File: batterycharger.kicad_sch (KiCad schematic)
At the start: 0 parts

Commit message: added
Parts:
- added U1: LT3652EMSE, Package_SO:MSOP-12-1EP_3x4mm_P0.65mm_EP1.65x2.85mm, symbol Battery_Management:LT3652EMSE
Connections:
- new net gnd: U1.13 (GND)
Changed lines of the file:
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@@
 (kicad_sch (version 20230121) (generator eeschema)
   (paper "A4")
-  (hierarchical_label "in" (shape input) (at 78.74 87.63 0) (fields_autoplaced)
+  (wire (pts (xy 63.5 107.95) (xy 87.63 107.95))
+    (stroke (width 0) (type default))
+  )
+  (wire (pts (xy 63.5 93.98) (xy 63.5 107.95))
+    (stroke (width 0) (type default))
+  )
+  (hierarchical_label "in" (shape input) (at 63.5 87.63 0) (fields_autoplaced)
     (effects (font (size 1.27 1.27)) (justify left))
   )
-  (hierarchical_label "load" (shape output) (at 95.25 87.63 0) (fields_autoplaced)
+  (hierarchical_label "gnd" (shape input) (at 63.5 93.98 0) (fields_autoplaced)
     (effects (font (size 1.27 1.27)) (justify left))
   )
+  (hierarchical_label "load" (shape output) (at 106.68 87.63 0) (fields_autoplaced)
+    (effects (font (size 1.27 1.27)) (justify left))
+  )
+  (symbol (lib_id "Battery_Management:LT3652EMSE") (at 87.63 95.25 0) (unit 1)
+    (in_bom yes) (on_board yes) (dnp no) (fields_autoplaced)
+    (property "Reference" "U1" (at 89.8241 80.01 0)
+      (effects (font (size 1.27 1.27)) (justify left))
+    )
+    (property "Value" "LT3652EMSE" (at 89.8241 82.55 0)
+      (effects (font (size 1.27 1.27)) (justify left))
+    )
+    (property "Footprint" "Package_SO:MSOP-12-1EP_3x4mm_P0.65mm_EP1.65x2.85mm" (at 87.63 110.49 0)
+      (effects (font (size 1.27 1.27)) hide)
+    )
+    (property "Datasheet" "https://www.analog.com/media/en/technical-documentation/data-sheets/3652fe.pdf" (at 102.87 115.57 0)
+      (effects (font (size 1.27 1.27)) hide)
+    )
+    (pin "1")
+    (pin "10")
+    (pin "11")
+    (pin "12")
+    (pin "13")
+    (pin "2")
+    (pin "3")
+    (pin "4")
+    (pin "5")
+    (pin "6")
+    (pin "7")
+    (pin "8")
+    (pin "9")
+    (instances
+      (project "eps"
+        (path "/d1becec8-2a81-45a7-bfc6-f9ad93456edc/a41c2f06-c716-4d4c-abbd-50372b3cec58"
+          (reference "U1") (unit 1)
+        )
+        (path "/d1becec8-2a81-45a7-bfc6-f9ad93456edc/98043307-5f00-404c-bb35-46ff24bbd3b8"
+          (reference "U2") (unit 1)
+        )
+      )
+    )
+  )
 )

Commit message: v0.1Hydrogen
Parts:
- added BT1, BT2, BT3, BT4: Battery_Cell, Battery:BatteryHolder_Keystone_1042_1x18650, symbol Device:Battery_Cell
- added C1, C4: 10uF, Capacitor_THT:C_Disc_D5.1mm_W3.2mm_P5.00mm, symbol Device:C
- added C2: 100uF, Capacitor_THT:CP_Radial_D6.3mm_P2.50mm, symbol Device:C_Polarized
- added C3: 1uF, Capacitor_THT:C_Disc_D5.0mm_W2.5mm_P2.50mm, symbol Device:C
- added C5: 100uF 16v, Capacitor_THT:CP_Radial_D6.3mm_P2.50mm, symbol Device:C_Polarized
- added D10, D9: LED, LED_THT:LED_Rectangular_W3.0mm_H2.0mm, symbol Device:LED
- added D11, D12, D13, D7, D8: 1N5819, Diode_THT:D_DO-41_SOD81_P10.16mm_Horizontal, symbol Diode:1N5819
- added J1: Barrel_Jack, Connector_BarrelJack:BarrelJack_SwitchcraftConxall_RAPC10U_Horizontal, symbol Connector:Barrel_Jack
- added L1: 68uH, Inductor_THT:L_Axial_L5.0mm_D3.6mm_P10.00mm_Horizontal_Murata_BL01RN1A2A2, symbol Device:L
- added R1: 568k, Resistor_THT:R_Axial_DIN0204_L3.6mm_D1.6mm_P5.08mm_Horizontal, symbol Device:R
- added R2, R3: 1k, Resistor_THT:R_Axial_DIN0204_L3.6mm_D1.6mm_P5.08mm_Horizontal, symbol Device:R
- added R4: 0.22, Resistor_THT:R_Axial_DIN0204_L3.6mm_D1.6mm_P5.08mm_Horizontal, symbol Device:R
- added R5: 0.5, Resistor_THT:R_Axial_DIN0204_L3.6mm_D1.6mm_P5.08mm_Horizontal, symbol Device:R
- added R6: 446k, Resistor_THT:R_Axial_DIN0204_L3.6mm_D1.6mm_P5.08mm_Horizontal, symbol Device:R
- added R7: 200k, Resistor_THT:R_Axial_DIN0204_L3.6mm_D1.6mm_P5.08mm_Horizontal, symbol Device:R
- added RV1: 10k, Potentiometer_THT:Potentiometer_Bourns_3386P_Vertical, symbol Device:R_Potentiometer
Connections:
- net gnd is gone; now on net GND: U1.13 (GND)
- net in: now also U1.1 (V_{IN}), U1.3 (~{SHDN}), C1.1, D10.2 (A), D12.2 (A), D7.1 (K), D9.2 (A), RV1.1
- net load: now also D12.1 (K), D13.1 (K)
- net at U1.10 (SENSE): now also L1.2, R4.1, R5.2
- net at U1.11 (BOOST): now also C3.1, D11.1 (K)
- net at U1.12 (SW): now also C3.2, D8.1 (K), L1.1
- net at U1.2 (V_{IN_REG}): now also RV1.2
- net chrg: now reaches U1.4 (~{CHRG})
- net chrg: now also R3.1
- net fault: now reaches U1.5 (~{FAULT})
- net fault: now also R2.1
- net GND: now reaches U1.6 (TIMER)
- net GND: now also BT3.2 (-), BT4.2 (-), C1.2, C2.2, C4.2, C5.2, D8.2 (A), J1.2, R6.2, RV1.3
- net at U1.7 (V_{FB}): now also R7.1
- net at U1.9 (BAT): now also BT1.1 (+), BT2.1 (+), C2.1, C4.1, C5.1, D11.2 (A), D13.2 (A), R1.1, R4.2, R5.1
- new net: D7.2 (A), J1.1
- new net: R1.2, R6.1, R7.2
- new net: D10.1 (K), R3.2
- new net: D9.1 (K), R2.2
- new net: BT2.2 (-), BT4.1 (+)
- new net: BT1.2 (-), BT3.1 (+)
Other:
- moved on the sheet: U1

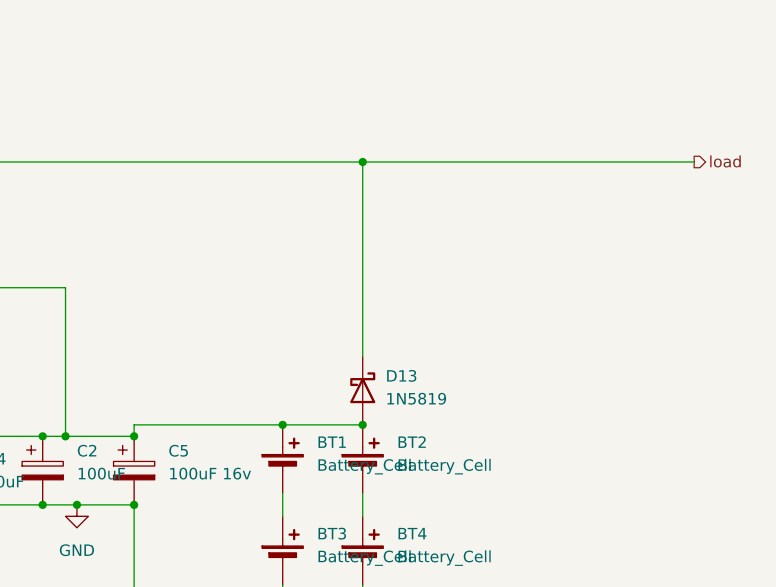
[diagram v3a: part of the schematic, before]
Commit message: Adding sensors
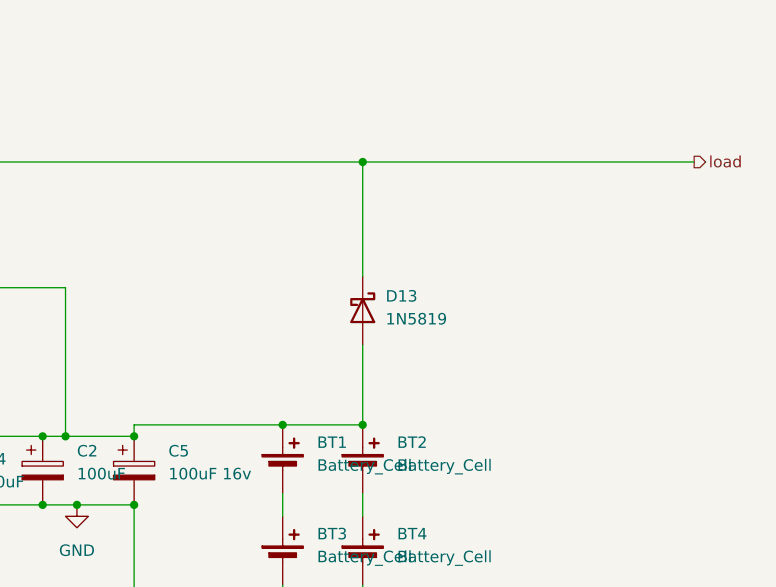
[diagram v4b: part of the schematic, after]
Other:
- moved on the sheet: D13
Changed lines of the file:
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@@
 	(wire
 		(pts
-			(xy 204.47 78.74) (xy 204.47 57.15)
+			(xy 204.47 69.85) (xy 204.47 57.15)
+		)
+		(stroke
+			(width 0)
+			(type default)
+		)
+	)
+	(wire
+		(pts
+			(xy 204.47 77.47) (xy 204.47 86.36)
 		)
 		(stroke
@@
 	(symbol
 		(lib_id "Diode:1N5819")
-		(at 204.47 82.55 270)
+		(at 204.47 73.66 270)
 		(unit 1)
 		(exclude_from_sim no)
@@
 		(fields_autoplaced yes)
 		(property "Reference" "D13"
-			(at 207.01 80.9625 90)
+			(at 207.01 72.0725 90)
 			(effects
 				(font
@@
 		)
 		(property "Value" "1N5819"
-			(at 207.01 83.5025 90)
+			(at 207.01 74.6125 90)
 			(effects
 				(font
@@
 		)
 		(property "Footprint" "Diode_THT:D_DO-41_SOD81_P10.16mm_Horizontal"
-			(at 200.025 82.55 0)
+			(at 200.025 73.66 0)
 			(effects
 				(font
@@
 		)
 		(property "Datasheet" "http://www.vishay.com/docs/88525/1n5817.pdf"
-			(at 204.47 82.55 0)
+			(at 204.47 73.66 0)
 			(effects
 				(font
@@
 		)
 		(property "Description" ""
-			(at 204.47 82.55 0)
-			(effects
-				(font
+			(at 204.47 73.66 0)
+			(effects
+				(font

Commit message: Added
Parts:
- added R8: R, Resistor_THT:R_Axial_DIN0204_L3.6mm_D1.6mm_P5.08mm_Horizontal, symbol Device:R
- added U2: INA234AxYBJ, Package_BGA:Texas_DSBGA-8_0.705x1.468mm_Layout2x4_P0.4mm, symbol Analog_ADC:INA234AxYBJ
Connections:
- net GND: now also U2.C2 (GND)
- net at BT1.1 (+), BT2.1 (+), C2.1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: now also R8.2, U2.B2 (IN-); no longer D13.2 (A)
- new net: D13.2 (A), R8.1, U2.A2 (IN+)
- new net +5V: U2.D2 (VS)
- new net a0: U2.B1 (A0)
- new net alert: U2.A1 (~{ALERT})
- new net scl: U2.D1 (SCL)
- new net sda: U2.C1 (SDA)
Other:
- moved on the sheet: D13

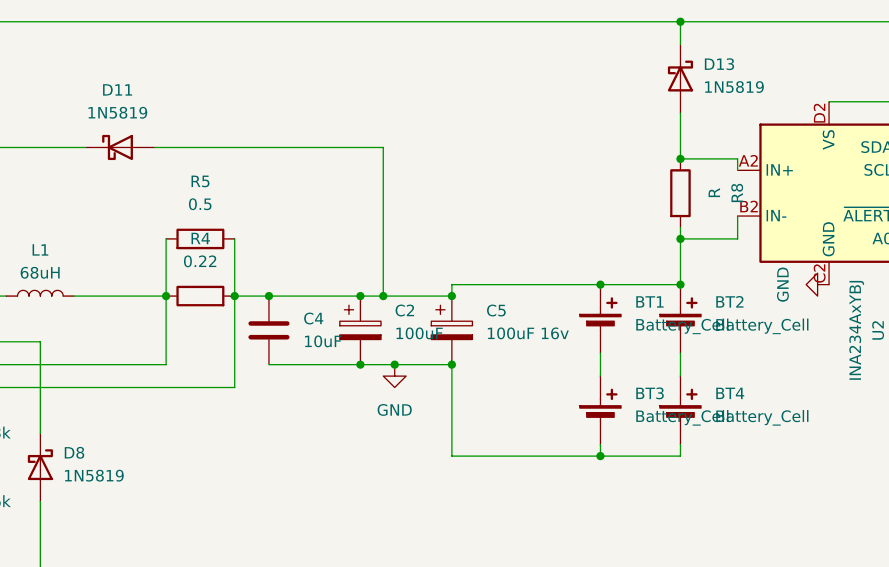
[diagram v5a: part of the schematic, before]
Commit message: changed placement
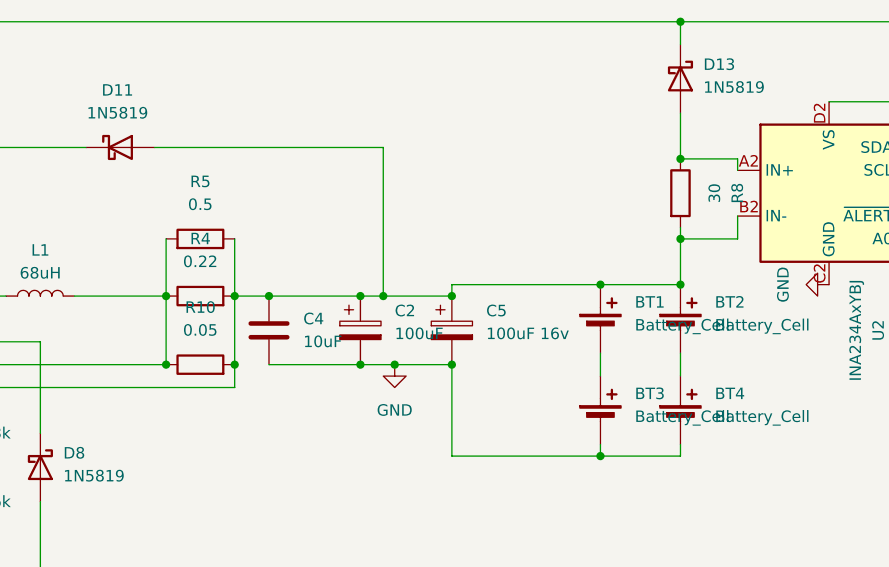
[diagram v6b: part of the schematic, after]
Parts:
- added R10: 0.05, symbol Device:R
- R8: value R -> 30
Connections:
- net at L1.2, R4.1, R5.2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: now also R10.1
- net at BT1.1 (+), BT2.1 (+), C2.1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: now also R10.2
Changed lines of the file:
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@@
+	)
+	(junction
+		(at 147.32 95.25)
+		(diameter 0)
+		(color 0 0 0 0)
 	)
 	(junction
@@
 	)
 	(junction
+		(at 154.94 95.25)
+		(diameter 0)
+		(color 0 0 0 0)
+	)
+	(junction
 		(at 123.19 97.79)
 		(diameter 0)
@@
 	(wire
 		(pts
-			(xy 154.94 97.79) (xy 154.94 87.63)
+			(xy 154.94 97.79) (xy 154.94 95.25)
 		)
 		(stroke
@@
 		(pts
 			(xy 49.53 69.85) (xy 49.53 74.93)
+		)
+		(stroke
+			(width 0)
+			(type default)
+		)
+	)
+	(wire
+		(pts
+			(xy 154.94 95.25) (xy 154.94 87.63)
 		)
 		(stroke
@@
 				(path "/d1becec8-2a81-45a7-bfc6-f9ad93456edc/a41c2f06-c716-4d4c-abbd-50372b3cec58"
 					(reference "R6")
+					(unit 1)
+				)
+			)
+		)
+	)
+	(symbol
+		(lib_id "Device:R")
+		(at 151.13 95.25 90)
+		(unit 1)
+		(exclude_from_sim no)
+		(in_bom yes)
+		(on_board yes)
+		(dnp no)
+		(fields_autoplaced yes)
+		(property "Reference" "R10"
+			(at 151.13 88.9 90)
+			(effects
+				(font
+					(size 1.27 1.27)
+				)
+			)
+		)
+		(property "Value" "0.05"
+			(at 151.13 91.44 90)
+			(effects
+				(font
+					(size 1.27 1.27)
+				)
+			)
+		)
+		(property "Footprint" ""
+			(at 151.13 97.028 90)
+			(effects
+				(font
+					(size 1.27 1.27)
+				)
+				(hide yes)
+			)
+		)
+		(property "Datasheet" "~"
+			(at 151.13 95.25 0)
+			(effects
+				(font
+					(size 1.27 1.27)
+				)
+				(hide yes)
+			)
+		)
+		(property "Description" "Resistor"
+			(at 151.13 95.25 0)
+			(effects
+				(font
+					(size 1.27 1.27)
+				)
+				(hide yes)
+			)
+		)
+		(pin "2"
+		)
+		(pin "1"
+		)
+		(instances
+			(project ""
+				(path "/d1becec8-2a81-45a7-bfc6-f9ad93456edc/a41c2f06-c716-4d4c-abbd-50372b3cec58"
+					(reference "R10")
 					(unit 1)
 				)
@@
 			)
 		)
-		(property "Value" "R"
+		(property "Value" "30"
 			(at 208.28 76.2 90)
 			(effects
